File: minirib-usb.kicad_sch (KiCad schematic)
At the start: 52 parts, among them J1 USB_B_Micro, J2 Mini-DIN-6-Shielded, Q1 MMST3904-7-F, Q2 MMST3906-7-F, Q3 MMST3906-7-F, Q4 MMST3904-7-F, Q5 MMST3904-7-F, Q6 MMST3904-7-F, Q7 MMST3904-7-F, U1 FT231XS, U2 TL081H

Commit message: finalized schematic for rev B
switched to CH340G for USB to serial operations due to supply chain issues with FTDI, and re-worked BUS- and /BUSY transistor arrangements to work properly without +15V RS232 as found in original schematic
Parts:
- removed U1: FT231XS, Package_SO:SSOP-20_3.9x8.7mm_P0.635mm, symbol Interface_USB:FT231XS
- added C10, C9: 0.1uF, Capacitor_SMD:C_0805_2012Metric_Pad1.18x1.45mm_HandSolder, symbol Device:C_Small
- added U1: CH340G, Package_SO:SOIC-16_3.9x9.9mm_P1.27mm, symbol Interface_USB:CH340G
- added Y1: 12MHz, Crystal:Crystal_SMD_SeikoEpson_FA238-4Pin_3.2x2.5mm_HandSoldering, symbol Device:Crystal_GND24_Small
- J2: value Mini-DIN-6-Shielded -> SB9600 Out
- gave numbers to parts that had none: 4
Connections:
- net +5V: now also R5.1, R6.2, U1.16 (VCC)
- net BUS+: now also D4.1 (A1); no longer D4.2 (A2)
- net BUSY: now also D3.1 (A1); no longer D3.2 (A2)
- net GND: now also C2.2, D3.2 (A2), D4.2 (A2), C10.2, C9.2, U1.1 (GND), Y1.2, Y1.4; no longer C2.1, D3.1 (A1), D4.1 (A1)
- net RXD: now also D6.1 (K), U1.3 (RXD)
- net TXD: now also D5.1 (K), U1.2 (TXD)
- net ~{CTS}: now also U1.11 (~{RI}), U1.9 (~{CTS})
- net ~{DTR}: now also U1.13 (~{DTR})
- net at R2.2: now also U1.6 (UD-)
- net at R1.1: now also U1.5 (UD+)
- net at R1.2: now also J1.3 (D+); no longer J1.2 (D-)
- net at R2.1: now also J1.2 (D-); no longer J1.3 (D+)
- removed net +3V3: C2.2, R5.1, R6.2
- new net: C2.1, U1.7 (XI), Y1.3
- new net: C9.1, U1.8 (XO), Y1.1
- new net: C10.1, U1.4 (V3)
- no-connect marks 6 -> 5
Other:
- moved on the sheet: C1, C4, D5, D6, J1, R1, R2, R5, R6

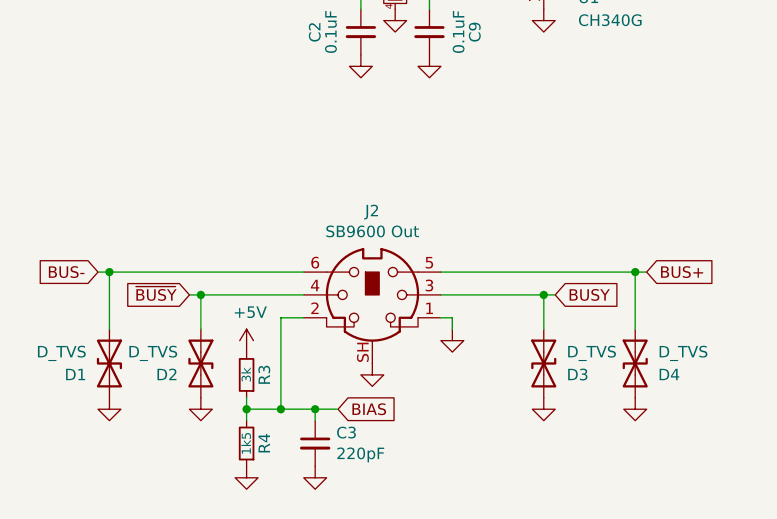
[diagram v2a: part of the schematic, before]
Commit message: switched to SC70 package for TL081
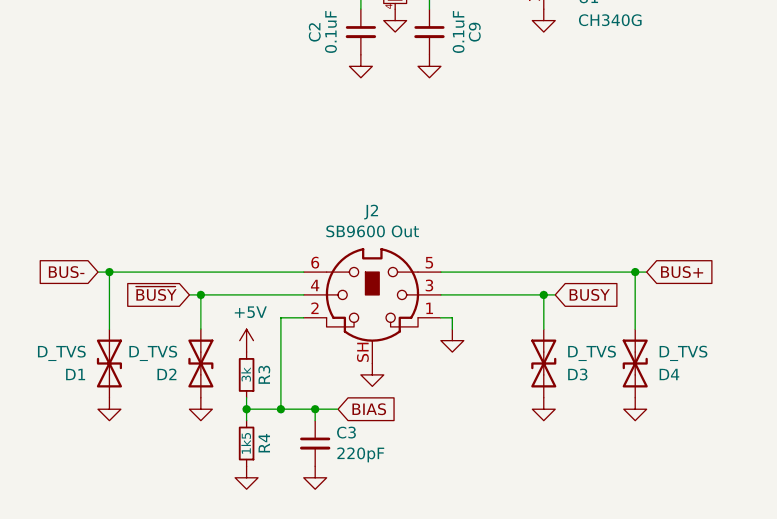
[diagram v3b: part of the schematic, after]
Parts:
- U2: footprint Package_TO_SOT_SMD:SOT-23-5_HandSoldering -> Package_TO_SOT_SMD:SOT-353_SC-70-5_Handsoldering
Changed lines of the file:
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@@
     (property "Reference" "U2" (id 0) (at 220.98 128.27 0))
     (property "Value" "TL081H" (id 1) (at 218.44 130.81 0))
-    (property "Footprint" "Package_TO_SOT_SMD:SOT-23-5_HandSoldering" (id 2) (at 222.25 133.35 0)
+    (property "Footprint" "Package_TO_SOT_SMD:SOT-353_SC-70-5_Handsoldering" (id 2) (at 222.25 133.35 0)
       (effects (font (size 1.27 1.27)) hide)
     )
@@
     )
     (path "/00000000-0000-0000-0000-000061cab525"
-      (reference "U2") (unit 1) (value "TL081H") (footprint "Package_TO_SOT_SMD:SOT-23-5_HandSoldering")
+      (reference "U2") (unit 1) (value "TL081H") (footprint "Package_TO_SOT_SMD:SOT-353_SC-70-5_Handsoldering")
     )
     (path "/b7ae2741-cdfb-4364-be17-bf0fe6f39ee4"

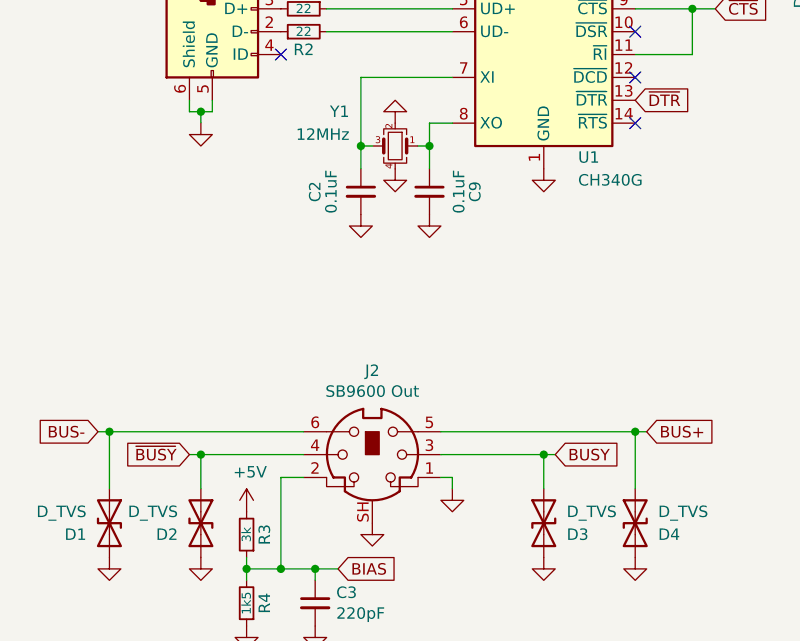
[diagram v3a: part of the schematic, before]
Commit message: added correct capacitors for crystal
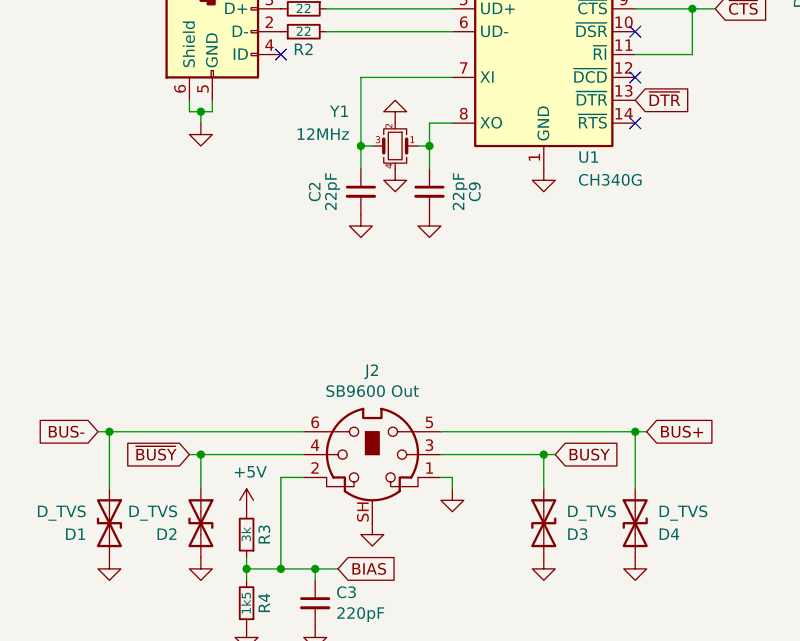
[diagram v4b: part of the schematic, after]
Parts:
- C2, C9: value 0.1uF -> 22pF
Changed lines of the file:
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@@
     (in_bom yes) (on_board yes)
     (property "Reference" "C2" (id 0) (at 69.85 93.98 90))
-    (property "Value" "0.1uF" (id 1) (at 72.39 93.98 90)
+    (property "Value" "22pF" (id 1) (at 72.39 93.98 90)
       (effects (font (size 1.27 1.27)) (justify bottom))
     )
@@
     (in_bom yes) (on_board yes)
     (property "Reference" "C9" (id 0) (at 87.63 93.98 90))
-    (property "Value" "0.1uF" (id 1) (at 85.09 93.98 90)
+    (property "Value" "22pF" (id 1) (at 85.09 93.98 90)
       (effects (font (size 1.27 1.27)) (justify bottom))
     )
@@
     )
     (path "/001e7031-5191-4137-b571-4db89e01d436"
-      (reference "C2") (unit 1) (value "0.1uF") (footprint "Capacitor_SMD:C_0805_2012Metric_Pad1.18x1.45mm_HandSolder")
+      (reference "C2") (unit 1) (value "22pF") (footprint "Capacitor_SMD:C_0805_2012Metric_Pad1.18x1.45mm_HandSolder")
     )
     (path "/00000000-0000-0000-0000-0000613a989a"
@@
     )
     (path "/8b8de74b-a6fb-4ed3-afed-26cf3e3e1736"
-      (reference "C9") (unit 1) (value "0.1uF") (footprint "Capacitor_SMD:C_0805_2012Metric_Pad1.18x1.45mm_HandSolder")
+      (reference "C9") (unit 1) (value "22pF") (footprint "Capacitor_SMD:C_0805_2012Metric_Pad1.18x1.45mm_HandSolder")
     )
     (path "/c4fbac00-9acb-4f3d-bb8e-e1bf130a776c"

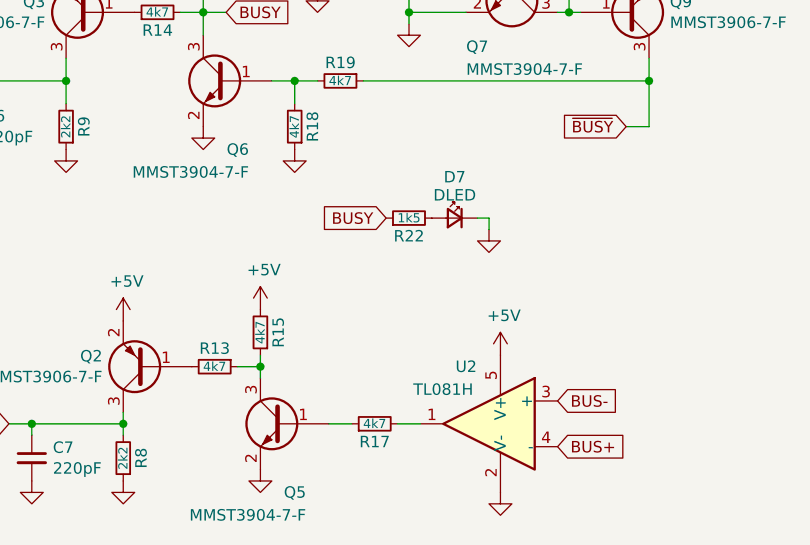
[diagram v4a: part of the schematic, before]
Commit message: schematic fixes based on rev B testing
- switched Opamp to MCP6491T to use correct footprint (SC70 footprint for TL081H is incorrect)
- Removed D7 BUSY LED as it was interfering with the proper signalling on the BUSY line
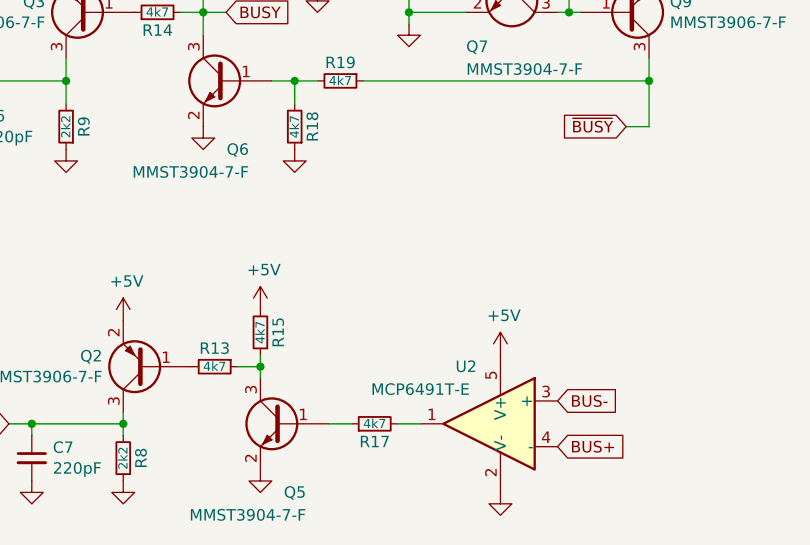
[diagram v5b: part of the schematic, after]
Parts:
- removed D7: DLED, Diode_SMD:D_0805_2012Metric_Pad1.15x1.40mm_HandSolder, symbol Device:LED_Small
- removed R22: 1k5, Resistor_SMD:R_0805_2012Metric_Pad1.20x1.40mm_HandSolder, symbol Device:R_Small
- U2: value TL081H -> MCP6491T-E
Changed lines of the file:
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@@
   (title_block
     (title "MiniRIB-USB")
-    (date "2022-01-04")
+    (date "2022-01-21")
     (rev "B")
     (company "W3AXL")
@@
     (stroke (width 0) (type default) (color 0 0 0 0))
   )
-  (wire (pts (xy 223.52 111.76) (xy 223.52 113.03))
-    (stroke (width 0) (type default) (color 0 0 0 0))
-  )
   (wire (pts (xy 66.04 135.89) (xy 69.85 135.89))
     (stroke (width 0) (type default) (color 0 0 0 0))
@@
   )
   (wire (pts (xy 74.93 88.9) (xy 76.2 88.9))
-    (stroke (width 0) (type default) (color 0 0 0 0))
-  )
-  (wire (pts (xy 222.25 111.76) (xy 223.52 111.76))
     (stroke (width 0) (type default) (color 0 0 0 0))
   )
@@
     )
   )
-  (global_label "BUSY" (shape input) (at 212.09 111.76 180) (fields_autoplaced)
-    (effects (font (size 1.27 1.27)) (justify right))
-    (property "Intersheet References" "${INTERSHEET_REFS}" (id 0) (at 0 0 0)
-      (effects (font (size 1.27 1.27)) hide)
-    )
-  )
   (global_label "RXD" (shape input) (at 170.18 134.62 180) (fields_autoplaced)
     (effects (font (size 1.27 1.27)) (justify right))
@@
     )
     (pin "1")
-  )
-  (symbol (lib_id "Device:LED_Small") (at 219.71 111.76 0) (mirror y) (unit 1)
-    (in_bom yes) (on_board yes)
-    (property "Reference" "D7" (id 0) (at 219.71 107.95 0)
-      (effects (font (size 1.27 1.27)) (justify bottom))
-    )
-    (property "Value" "DLED" (id 1) (at 219.71 109.22 0))
-    (property "Footprint" "Diode_SMD:D_0805_2012Metric_Pad1.15x1.40mm_HandSolder" (id 2) (at 219.71 111.76 90)
-      (effects (font (size 1.27 1.27)) hide)
-    )
-    (property "Datasheet" "~" (id 3) (at 219.71 111.76 90)
-      (effects (font (size 1.27 1.27)) hide)
-    )
-    (pin "1")
-    (pin "2")
-  )
-  (symbol (lib_id "Device:R_Small") (at 214.63 111.76 90) (unit 1)
-    (in_bom yes) (on_board yes)
-    (property "Reference" "R22" (id 0) (at 214.63 113.03 90)
-      (effects (font (size 1.27 1.27)) (justify bottom))
-    )
-    (property "Value" "1k5" (id 1) (at 214.63 111.76 90)
-      (effects (font (size 1.016 1.016)))
-    )
-    (property "Footprint" "Resistor_SMD:R_0805_2012Metric_Pad1.20x1.40mm_HandSolder" (id 2) (at 214.63 111.76 0)
-      (effects (font (size 1.27 1.27)) hide)
-    )
-    (property "Datasheet" "~" (id 3) (at 214.63 111.76 0)
-      (effects (font (size 1.27 1.27)) hide)
-    )
-    (pin "1")
-    (pin "2")
   )
   (symbol (lib_id "Device:LED_Small") (at 128.27 72.39 90) (unit 1)
@@
     (pin "3")
   )
-  (symbol (lib_id "power:GND") (at 223.52 113.03 0) (unit 1)
-    (in_bom yes) (on_board yes)
-    (property "Reference" "#PWR010" (id 0) (at 223.52 119.38 0)
-      (effects (font (size 1.27 1.27)) hide)
-    )
-    (property "Value" "GND" (id 1) (at 223.647 117.4242 0)
-      (effects (font (size 1.27 1.27)) hide)
-    )
-    (property "Footprint" "" (id 2) (at 223.52 113.03 0)
-      (effects (font (size 1.27 1.27)) hide)
-    )
-    (property "Datasheet" "" (id 3) (at 223.52 113.03 0)
-      (effects (font (size 1.27 1.27)) hide)
-    )
-    (pin "1")
-  )
   (symbol (lib_id "MiniDin:TL081H") (at 223.52 134.62 0) (mirror y) (unit 1)
     (in_bom yes) (on_board yes)
     (property "Reference" "U2" (id 0) (at 220.98 128.27 0))
-    (property "Value" "TL081H" (id 1) (at 218.44 130.81 0))
+    (property "Value" "MCP6491T-E" (id 1) (at 215.9 130.81 0))
     (property "Footprint" "Package_TO_SOT_SMD:SOT-353_SC-70-5_Handsoldering" (id 2) (at 222.25 133.35 0)
       (effects (font (size 1.27 1.27)) hide)
@@
       (reference "#PWR09") (unit 1) (value "GND") (footprint "")
     )
-    (path "/00000000-0000-0000-0000-000061c914cd"
-      (reference "#PWR010") (unit 1) (value "GND") (footprint "")
-    )
     (path "/00000000-0000-0000-0000-0000611a49b5"
       (reference "#PWR011") (unit 1) (value "GND") (footprint "")
@@
       (reference "D6") (unit 1) (value "RXLED") (footprint "Diode_SMD:D_0805_2012Metric_Pad1.15x1.40mm_HandSolder")
     )
-    (path "/00000000-0000-0000-0000-000061418ae2"
-      (reference "D7") (unit 1) (value "DLED") (footprint "Diode_SMD:D_0805_2012Metric_Pad1.15x1.40mm_HandSolder")
-    )
     (path "/00000000-0000-0000-0000-000061bb19cd"
       (reference "J1") (unit 1) (value "USB_B_Micro") (footprint "Connector_USB:USB_Micro-B_Wuerth_629105150521")
@@
       (reference "R21") (unit 1) (value "20k") (footprint "Resistor_SMD:R_0805_2012Metric_Pad1.20x1.40mm_HandSolder")
     )
-    (path "/00000000-0000-0000-0000-00006141acf7"
-      (reference "R22") (unit 1) (value "1k5") (footprint "Resistor_SMD:R_0805_2012Metric_Pad1.20x1.40mm_HandSolder")
-    )
     (path "/00000000-0000-0000-0000-000061d6c85b"
       (reference "R23") (unit 1) (value "4k7") (footprint "Resistor_SMD:R_0805_2012Metric_Pad1.20x1.40mm_HandSolder")
@@
     )
     (path "/00000000-0000-0000-0000-000061cab525"
-      (reference "U2") (unit 1) (value "TL081H") (footprint "Package_TO_SOT_SMD:SOT-353_SC-70-5_Handsoldering")
+      (reference "U2") (unit 1) (value "MCP6491T-E") (footprint "Package_TO_SOT_SMD:SOT-353_SC-70-5_Handsoldering")
     )
     (path "/b7ae2741-cdfb-4364-be17-bf0fe6f39ee4"
